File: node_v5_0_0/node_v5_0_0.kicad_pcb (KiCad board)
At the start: 4 copper layers, 102 parts, among them J1 Conn_01x02_Pin, J10 Connector, USB-TYPE-C-16P, J3 Conn_Coaxial, J4 Conn_02x08_Odd_Even, J5 Conn_02x02_Odd_Even, J6 GNSS_ANT, J7 RF_ANT, J8 Conn_01x02_Pin, J9 Conn_Coaxial, Q1 DMG2301L, Q2 DMG2301L, SW1 PTS636 SM50J SMTR LFS, SW2 PTS636 SM50J SMTR LFS, SW3 PTS636 SM50J SMTR LFS, U1 RP2040, U10 MCP7940 / DS1307 / PCF8523, U11 1042240820, U12 CAT24M01W, U13 MAX31342EWA+T, U14 W25Q128, U2 USBLC6-2SC6, U3 AP2112K-3.3, U4 CAT3200-5, U5 MCP73831-2-OT, U6 RFM69HCW, U9 SIM7080G

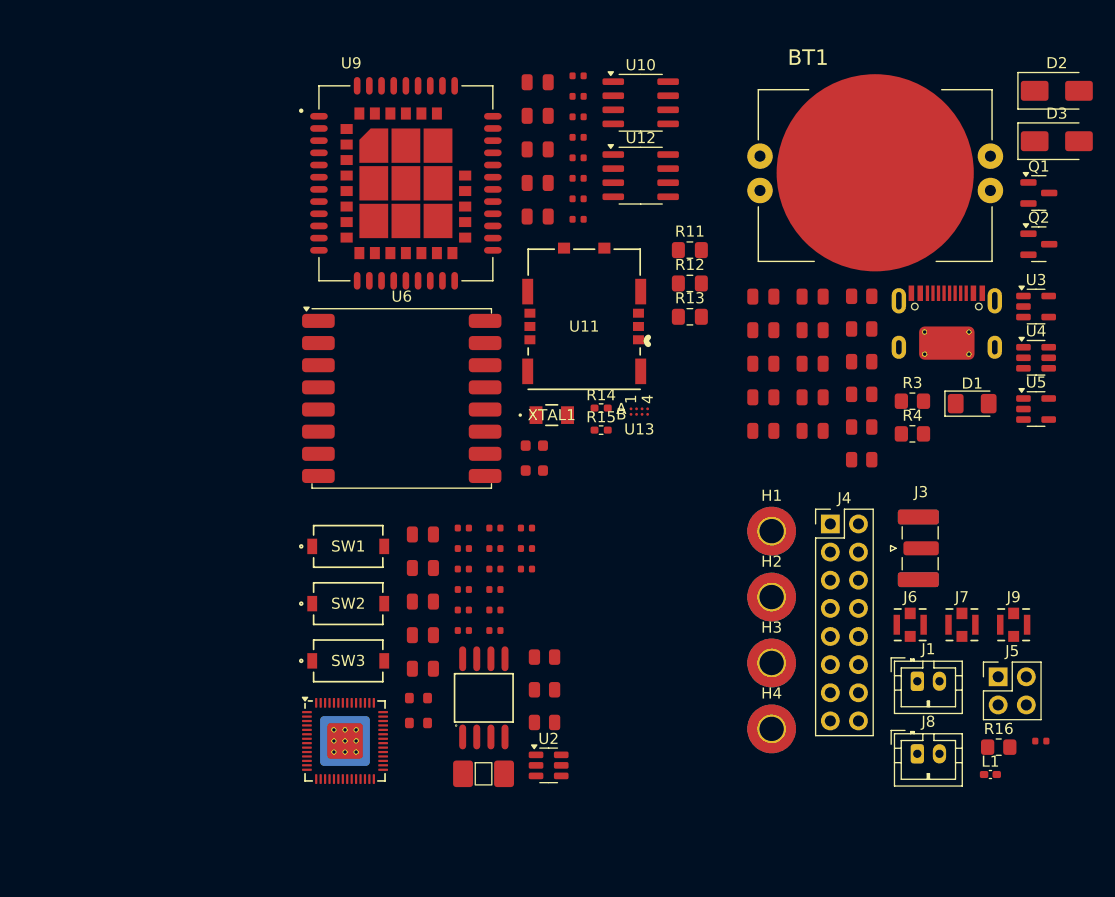
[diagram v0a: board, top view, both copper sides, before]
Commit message: updated layout
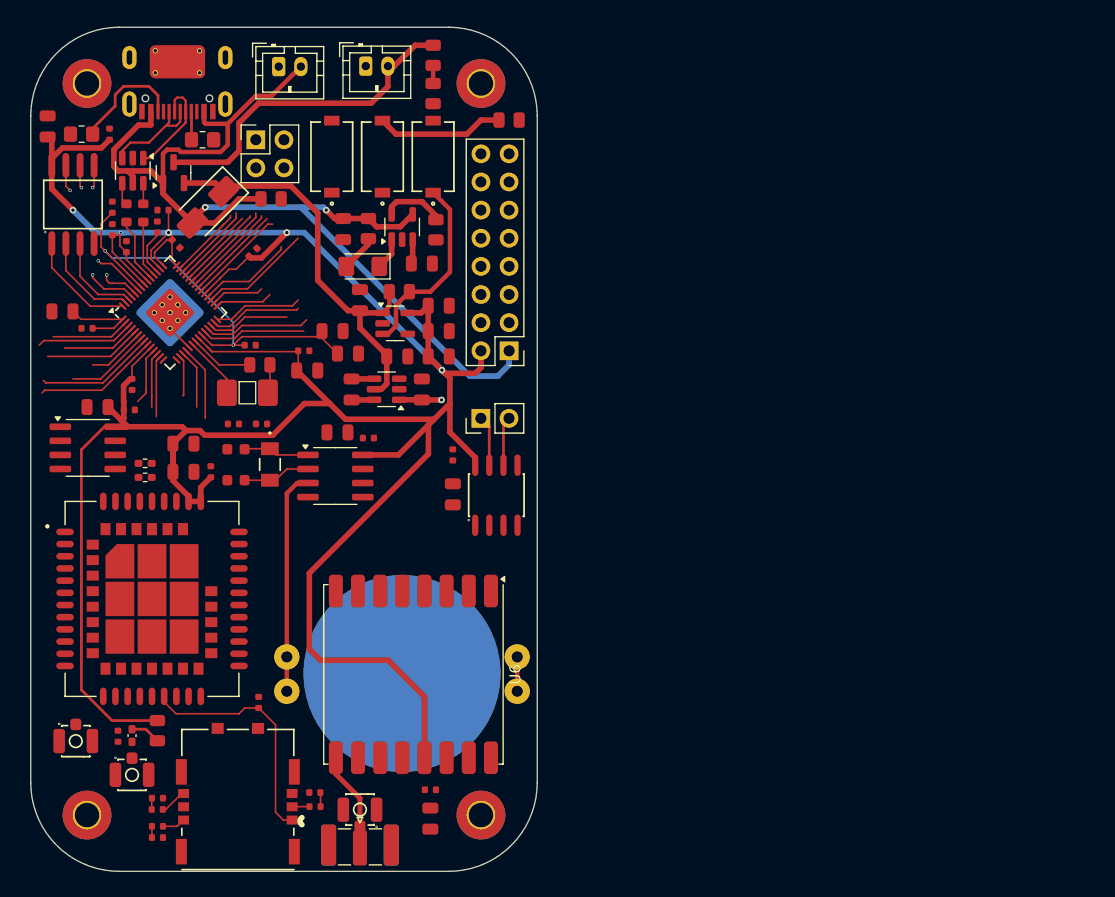
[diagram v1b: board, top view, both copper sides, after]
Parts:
- removed C46: 10u, JLCPCB-Kicad-Footprints:C_0805
- removed C9: 0.1u, JLCPCB-Kicad-Footprints:C_0402
- removed D3: SS14, Diode_SMD:D_SMA
- removed Q2: DMG2301L, Package_TO_SOT_SMD:SOT-23
- removed R19: 10k, JLCPCB-Kicad-Footprints:R_0805
- removed U10: MCP7940 / DS1307 / PCF8523, Package_SO:SOIC-8_3.9x4.9mm_P1.27mm
- removed U13: MAX31342EWA+T, WiSDOM:21-100291_W80D&plus_1_MXM
- added C17: 0.1u, JLCPCB-Kicad-Footprints:C_0402, F.Cu at (64.3, 64.6)
- added C18: 10u, JLCPCB-Kicad-Footprints:C_0805, F.Cu at (64.3, 68.1)
- added J2: U.FL, JLCPCB-Kicad-Footprints:IPEX-SMD_BWIPX-1-001E, F.Cu at (55.9, 97.4)
- added U7: PCF8523T, Package_SO:SOIC-8_3.9x4.9mm_P1.27mm, F.Cu at (53.7, 66.5)
- added U8: SP3485EN, JLCPCB-Kicad-Footprints:SOIC-8_L5.0-W4.0-P1.27-LS6.0-BL, F.Cu at (68.2, 68.2)
- BT1: value RTC_BAT -> Battery_Cell; moved to B.Cu
- D2: footprint Diode_SMD:D_SMA -> JLCPCB-Kicad-Footprints:D_SMA
- J6: value GNSS_ANT -> U.FL; footprint WiSDOM:CONN_CONMHF1-SMD_LNX -> JLCPCB-Kicad-Footprints:IPEX-SMD_BWIPX-1-001E
- J7: value RF_ANT -> Conn_01x02_Pin; footprint WiSDOM:CONN_CONMHF1-SMD_LNX -> Connector_PinHeader_2.54mm:PinHeader_1x02_P2.54mm_Vertical
- J9: value Conn_Coaxial -> U.FL; footprint WiSDOM:CONN_CONMHF1-SMD_LNX -> JLCPCB-Kicad-Footprints:IPEX-SMD_BWIPX-1-001E
- L1: value L -> 68nH
- R11, R12, R13: footprint Capacitor_SMD:C_0805_2012Metric_Pad1.18x1.45mm_HandSolder -> JLCPCB-Kicad-Footprints:R_0402
- R16: footprint Resistor_SMD:R_0805_2012Metric_Pad1.20x1.40mm_HandSolder -> JLCPCB-Kicad-Footprints:R_0805
- moved J8 84.7 mm to (48.6, 29.5)
- moved C43 83.3 mm to (34.0, 90.0), turned to -90 degrees
- moved J5 82.7 mm to (46.5, 36.1)
- moved J9 80.6 mm to (35.3, 92.7), turned to -90 degrees
- moved R4 79.7 mm to (30.8, 35.6), turned to 180 degrees
- moved Q1 78.1 mm to (39.1, 39.1), turned to 90 degrees
- moved L1 77.6 mm to (35.3, 89.9), turned to -90 degrees
- moved D2 77.3 mm to (42.2, 42.2), turned to -135 degrees
- moved R16 76.0 mm to (37.6, 89.5), turned to -90 degrees
- moved J6 76.0 mm to (30.2, 89.7), turned to -90 degrees
- moved J1 74.6 mm to (56.4, 29.5)
- moved H1 73.8 mm to (31.3, 31.1)
- moved C35 73.7 mm to (37.6, 99.1)
- moved J10 72.7 mm to (39.4, 31.1), turned to 180 degrees
- moved C36 69.2 mm to (37.6, 95.6)
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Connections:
- BT1 pad 1: RTC_BAT -> Net-(BT1-+)
- C43 pad 2: Net-(J6-In) -> Net-(J9-In)
- J6 pad 1: Net-(J6-In) -> LTE_ANT
- J7 pad 1: RF_ANT -> 485-
- J7 pad 2: GND -> 485+
- J9 pad 1: RFM_ANT -> Net-(J9-In)
- L1 pad 2: Net-(J6-In) -> Net-(J9-In)
- U1 pad 13: unconnected-(U1-GPIO10-Pad13) -> RFM_DIO0
- U1 pad 14: unconnected-(U1-GPIO11-Pad14) -> RFM_DIO1
- U1 pad 34: unconnected-(U1-GPIO22-Pad34) -> RFM_DIO2
- U1 pad 35: unconnected-(U1-GPIO23-Pad35) -> RFM_DIO3
- U1 pad 36: unconnected-(U1-GPIO24-Pad36) -> RFM_DIO4
- U1 pad 37: unconnected-(U1-GPIO25-Pad37) -> RFM_DIO5
- U1 pad 8: unconnected-(U1-GPIO6-Pad8) -> 485_DE
- U1 pad 9: unconnected-(U1-GPIO7-Pad9) -> 485_!RE
- U2 pad 1: USB+ -> USB-
- U2 pad 3: USB- -> USB+
- U2 pad 4: /MCU/D- -> /MCU/D+
- U2 pad 6: /MCU/D+ -> /MCU/D-
- U6 pad 11: unconnected-(U6-DIO3-Pad11) -> RFM_DIO3
- U6 pad 12: unconnected-(U6-DIO4-Pad12) -> RFM_DIO4
- U6 pad 14: unconnected-(U6-DIO0-Pad14) -> RFM_DIO0
- U6 pad 15: unconnected-(U6-DIO1-Pad15) -> RFM_DIO1
- U6 pad 16: unconnected-(U6-DIO2-Pad16) -> RFM_DIO2
- U6 pad 7: unconnected-(U6-DIO5-Pad7) -> RFM_DIO5
- U9 pad 32: RF_ANT -> LTE_ANT
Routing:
- net +3.3V: track 0.00 -> 276.6 mm, vias 0 -> 5
- net VBUS: track 0.00 -> 96.5 mm, vias 0 -> 2
- net +1V1: track 0.00 -> 44.6 mm, vias 0 -> 2
- net +VSW: track 0.00 -> 37.9 mm
- net +BATT: track 0.00 -> 32.6 mm
- net Net-(BT1-+): track 0.00 -> 23.3 mm
- net /PERIPHERALS/SIM_VCC: track 0.00 -> 21.5 mm
- net 3VEN: track 0.00 -> 17.3 mm
- net /MCU/CLK: track 0.00 -> 14.9 mm, vias 0 -> 2
- net /MCU/D3: track 0.00 -> 14.5 mm, vias 0 -> 2
- net /MCU/D0: track 0.00 -> 14.5 mm, vias 0 -> 2
- net +5V: track 0.00 -> 12.5 mm, vias 0 -> 1
- net Net-(R10-Pad1): track 0.00 -> 11.6 mm
- net 485_!RE: track 0.00 -> 11.4 mm
- net 485_DE: track 0.00 -> 10.8 mm
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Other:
- board outline added: 45.7 x 76.2 mm

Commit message: lots of routing
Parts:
- added REF**: KiCad-Logo2_6mm_SilkScreen, Symbol:KiCad-Logo2_6mm_SilkScreen, B.Cu at (42.0, 97.1)
- added REF**: OSHW-Logo_5.7x6mm_SilkScreen, Symbol:OSHW-Logo_5.7x6mm_SilkScreen, B.Cu at (31.2, 90.9)
- moved C47 0.56 mm to (28.1, 34.5)
- moved R4 0.49 mm to (31.0, 35.2)
- moved U6 0.41 mm to (60.3, 84.4)
- moved C20 0.32 mm to (47.2, 61.6)
- moved C2 0.27 mm to (34.5, 45.8)
- moved C19 0.23 mm to (44.4, 61.6)
- turned U9 to 180 degrees
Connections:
- J2 pad 3: (no net) -> GND
- J6 pad 3: (no net) -> GND
- J9 pad 3: (no net) -> GND
- U11 pad 11: (no net) -> GND
- U11 pad 12: (no net) -> GND
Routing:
- net SDA: track 5.24 -> 90.1 mm, vias 0 -> 5
- net SCL: track 7.71 -> 92.5 mm, vias 0 -> 4
- net /PERIPHERALS/SIM_CLK: track 1.02 -> 76.7 mm, vias 0 -> 2
- net GND: track 3.93 -> 76.8 mm, vias 0 -> 52
- net RFM_DIO3: track 8.77 -> 78.5 mm, vias 0 -> 2
- net RFM_DIO2: track 8.90 -> 78.0 mm, vias 0 -> 2
- net TX1: track 5.20 -> 71.7 mm, vias 0 -> 2
- net RX1: track 5.02 -> 71.5 mm, vias 0 -> 2
- net MISO: track 8.38 -> 71.4 mm, vias 0 -> 3
- net RFM_DIO4: track 8.65 -> 70.3 mm, vias 0 -> 2
- net SPI_CK: track 5.18 -> 66.5 mm, vias 0 -> 3
- net RFM_DIO1: track 0.00 -> 52.3 mm, vias 0 -> 3
- net MOSI: track 4.80 -> 56.9 mm, vias 0 -> 4
- net RFM_DIO0: track 5.53 -> 57.5 mm, vias 0 -> 2
- net 485_DE: track 10.8 -> 61.9 mm, vias 0 -> 2
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- added copper zone on B.Cu, net GND
- added copper zone on F.Cu, net GND
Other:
- board text added: "+"
- board text added: "-"
- board text added: "12MHz"
- board text added: "32kHz"
- board text added: "3V3"
- board text added: "5V"
- board text added: "AP2112"
- board text added: "BAT"
- board text added: "BOOTSEL"
- board text added: "C1"
- board text added: "C10"
- board text added: "C11"
- board text added: "C12"
- board text added: "C13"
- board text added: "C14"
- board text added: "C15"
- board text added: "C16"
- board text added: "C17"
- board text added: "C18"
- board text added: "C19"
- board text added: "C2"
- board text added: "C20"
- board text added: "C21"
- board text added: "C22"
- board text added: "C23"
- board text added: "C24"
- board text added: "C25"
- board text added: "C26"
- board text added: "C27"
- board text added: "C28"
- board text added: "C29"
- board text added: "C3"
- board text added: "C30"
- board text added: "C31"
- board text added: "C32"
- board text added: "C33"
- board text added: "C34"
- board text added: "C35"
- board text added: "C36"
- board text added: "C37"
- board text added: "C38"
- board text added: "C39"
- board text added: "C4"
- board text added: "C40"
- board text added: "C41"
- board text added: "C42"
- board text added: "C43"
- board text added: "C44"
- board text added: "C45"
- board text added: "C47"
- board text added: "C48"
- board text added: "C5"
- board text added: "C6"
- board text added: "C7"
- board text added: "C8"
- board text added: "CAT24M01W"
- board text added: "CAT3200-5"
- board text added: "CHG"
- board text added: "CLK"
- board text added: "CS"
- board text added: "DMG2301"
- board text added: "GND"
- board text added: "GNSS"
- board text added: "GP27"
- board text added: "GP28"
- board text added: "GP29"
- board text added: "L1"
- board text added: "LTE CAT-M NB-IOT"
- board text added: "MCP73831"
- board text added: "MISO"
- board text added: "MOSI"
- board text added: "PCF8523"
- board text added: "R1"
- board text added: "R10"
- board text added: "R11"
- board text added: "R12"
- board text added: "R13"
- board text added: "R14"
- board text added: "R15"
- board text added: "R16"
- board text added: "R17"
- board text added: "R18"
- board text added: "R2"
- board text added: "R3"
- board text added: "R4"
- board text added: "R5"
- board text added: "R6"
- board text added: "R7"
- board text added: "R8"
- board text added: "R9"
- board text added: "RFM69HCW"
- board text added: "RP2040"
- board text added: "RS 485"
- board text added: "RST"
- board text added: "RUN"
- board text added: "RX1"
- board text added: "SCL"
- board text added: "SDA"
- board text added: "SIM7080G"
- board text added: "SP3485"
- board text added: "SS14"
- board text added: "SWCLK"
- board text added: "SWD"
- board text added: "TX1"
- board text added: "USB 2.0"
- board text added: "USBLC6-2"
- board text added: "VBUS"
- board text added: "W25Q128"

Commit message: drc time
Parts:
- moved J5 0.49 mm to (46.9, 35.8)
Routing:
- net +3.3V: track 301.1 -> 301.6 mm
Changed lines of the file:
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@@
 	(footprint "Connector_PinHeader_2.54mm:PinHeader_2x02_P2.54mm_Vertical"
 		(layer "F.Cu")
-		(at 46.496 36.144)
+		(at 46.863 35.814)
 		(descr "Through hole straight pin header, 2x02, 2.54mm pitch, double rows")
 		(tags "Through hole pin header THT 2x02 2.54mm double row")
@@
 		(layer "F.Cu")
 		(at 58.3015 58.666 180)
-		(descr "SOT, 6 Pin (https://www.jedec.org/sites/default/files/docs/Mo-178c.PDF variant AB), generated with kicad-footprint-generator ipc_gullwing_generator.py")
+		(descr "SOT, 6 Pin (JEDEC MO-178 Var AB https://www.jedec.org/document_search?search_api_views_fulltext=MO-178), generated with kicad-footprint-generator ipc_gullwing_generator.py")
 		(tags "SOT TO_SOT_SMD")
 		(property "Reference" "U4"
-			(at 0 -2.4 0)
+			(at 0 -2.4 180)
 			(layer "F.SilkS")
 			(hide yes)
@@
 		)
 		(property "Value" "CAT3200-5"
-			(at 0 2.4 0)
+			(at 0 2.4 180)
 			(layer "F.Fab")
 			(hide yes)
@@
 		(property "Footprint" "Package_TO_SOT_SMD:SOT-23-6"
 			(at 0 0 180)
-			(unlocked yes)
 			(layer "F.Fab")
 			(hide yes)
@@
 		(property "Datasheet" "https://www.onsemi.com/pdf/datasheet/cat3200-d.pdf"
 			(at 0 0 180)
-			(unlocked yes)
 			(layer "F.Fab")
 			(hide yes)
@@
 		(property "Description" "Low Noise Regulated Charge Pump DC-DC Converter, 5 V, 100 mA, SOT-23-6"
 			(at 0 0 180)
-			(unlocked yes)
 			(layer "F.Fab")
 			(hide yes)
@@
 		)
 		(fp_text user "${REFERENCE}"
-			(at 0 0 0)
+			(at 0 0 180)
 			(layer "F.Fab")
 			(effects
@@
 	)
 	(segment
-		(start 45.7508 37.3972)
-		(end 38.622 44.526)
+		(start 38.622 44.526)
+		(end 46.0472 37.1008)
 		(width 0.4064)
 		(layer "In2.Cu")
@@
 	)
 	(segment
-		(start 47.7828 37.3972)
-		(end 45.7508 37.3972)
+		(start 48.1162 37.1008)
+		(end 49.403 35.814)
 		(width 0.4064)
 		(layer "In2.Cu")
@@
 	)
 	(segment
-		(start 49.036 36.144)
-		(end 47.7828 37.3972)
+		(start 46.0472 37.1008)
+		(end 48.1162 37.1008)
 		(width 0.4064)
 		(layer "In2.Cu")
@@
 	(segment
 		(start 46.496 43.155471)
-		(end 46.496 38.684)
+		(end 46.496 42.835817)
+		(width 0.1524)
+		(layer "In1.Cu")
+		(net 37)
+	)
+	(segment
+		(start 46.863 42.468817)
+		(end 46.863 38.354)
 		(width 0.1524)
 		(layer "In1.Cu")
@@
 	)
 	(segment
+		(start 46.496 42.835817)
+		(end 46.863 42.468817)
+		(width 0.1524)
+		(layer "In1.Cu")
+		(net 37)
+	)
+	(segment
 		(start 45.8216 43.829871)
 		(end 46.496 43.155471)
@@
 	)
 	(segment
-		(start 46.1772 49.346583)
-		(end 46.1772 43.97264)
+		(start 47.9892 36.9402)
+		(end 46.863 35.814)
 		(width 0.1524)
 		(layer "In1.Cu")
@@
 	)
 	(segment
-		(start 47.6222 37.2702)
-		(end 46.496 36.144)
+		(start 46.1772 49.346583)
+		(end 46.1772 43.97264)
 		(width 0.1524)
 		(layer "In1.Cu")
@@
 	)
 	(segment
-		(start 47.6222 42.52764)
-		(end 47.6222 37.2702)
+		(start 47.9892 42.16064)
+		(end 47.9892 36.9402)
 		(width 0.1524)
 		(layer "In1.Cu")
@@
 	(segment
 		(start 46.1772 43.97264)
-		(end 47.6222 42.52764)
+		(end 47.9892 42.16064)
 		(width 0.1524)
 		(layer "In1.Cu")

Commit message: finished layout and routing?
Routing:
- net +3.3V: track 301.6 -> 310.1 mm, vias 5 -> 6
- net +1V1: track 44.6 -> 48.8 mm, vias 2 -> 3
- net GND: vias 52 -> 53

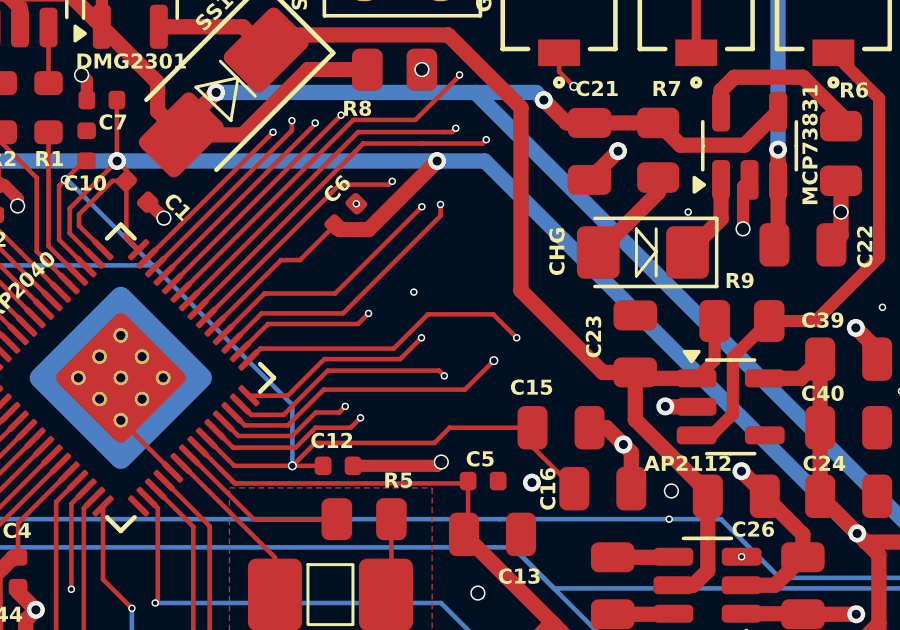
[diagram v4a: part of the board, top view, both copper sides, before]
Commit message: updated layout of silkscreen, added labels and qr codes
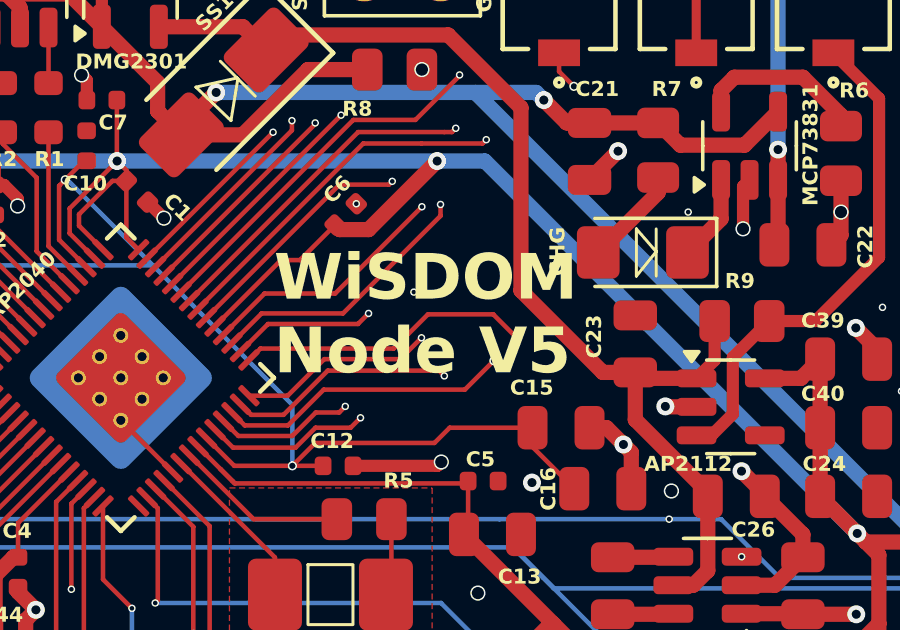
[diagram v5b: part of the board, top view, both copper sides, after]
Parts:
- added G***: LOGO, WiSDOM:wisdomcatnomow, B.Cu at (42.7, 68.0)
- added G***: LOGO, WiSDOM:vtsu, B.Cu at (60.5, 65.7)
- added G***: LOGO, logos:wisdom_logo_lineborder, B.Cu at (46.0, 46.0)
- added LOGO: , logos:github_qr, B.Cu at (37.7, 89.0)
- added LOGO: , logos:qrcode, B.Cu at (46.4, 89.0)
- moved REF** 19.4 mm to (30.5, 71.5)
- moved REF** 1.84 mm to (42.0, 95.2)
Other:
- board text added: "Schematic & PCB design by amelia vlahogiannis Jan. 2025"
- board text added: "WiSDOM Node V5"
- board text added: "wisdomresearch.net github.com/VTC-WISDOM"
